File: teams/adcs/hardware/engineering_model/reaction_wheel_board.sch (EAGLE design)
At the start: 81 parts

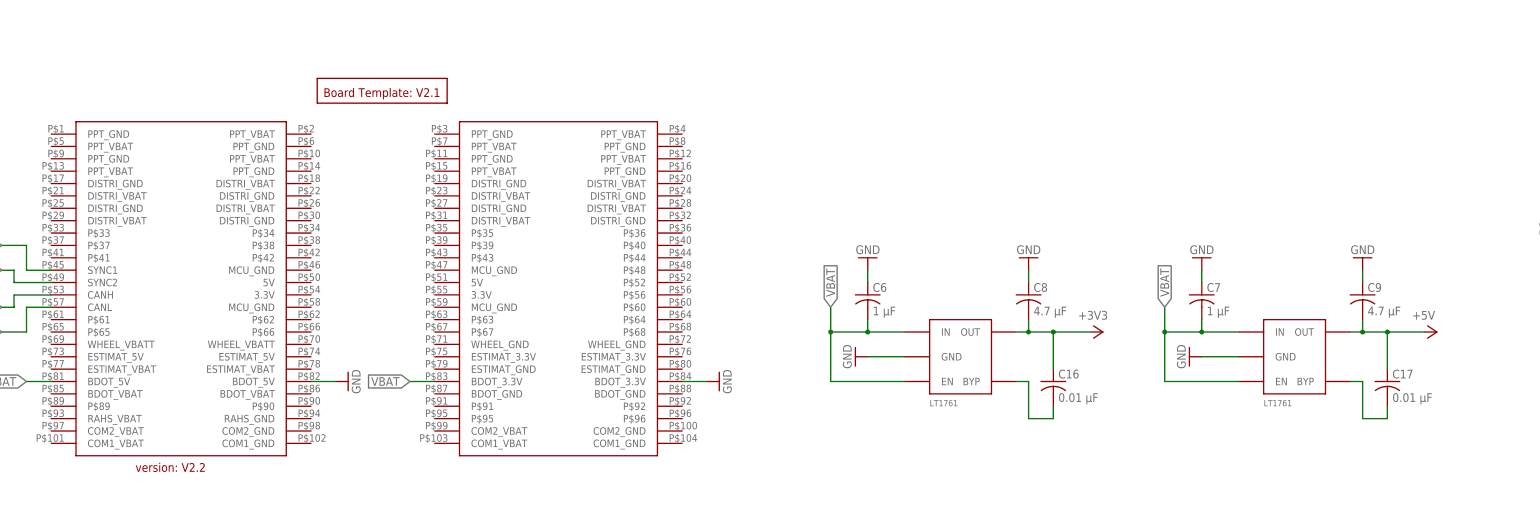
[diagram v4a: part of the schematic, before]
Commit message: ADCS: Fix broken git remote
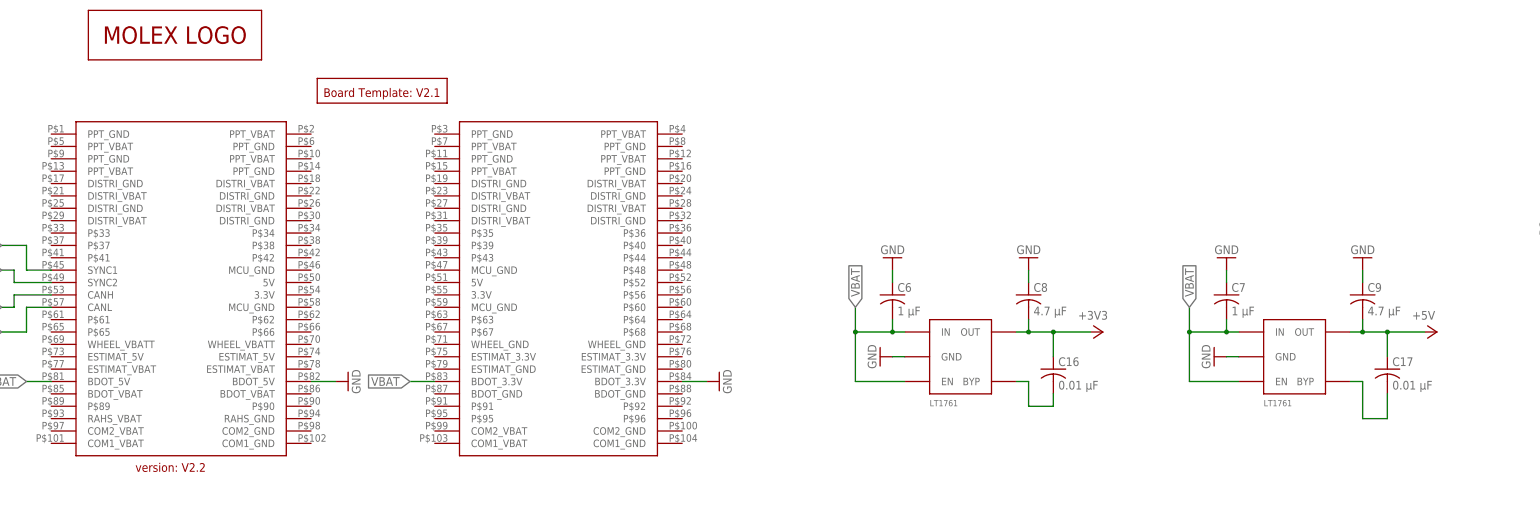
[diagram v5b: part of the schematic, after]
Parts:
- added U$8: LOGO_MOLEX, HuskySat-1 Logos:LOGO_MOLEX
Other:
- moved on the sheet: C16, C17, C6, C7
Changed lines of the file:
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@@
 <?xml version="1.0" encoding="utf-8"?>
 <!DOCTYPE eagle SYSTEM "eagle.dtd">
-<eagle version="8.3.2">
+<eagle version="8.4.1">
 <drawing>
 <settings>
@@
 <layer number="59" name="tCarbon" color="7" fill="1" visible="no" active="no"/>
 <layer number="60" name="bCarbon" color="7" fill="1" visible="no" active="no"/>
+<layer number="88" name="SimResults" color="9" fill="1" visible="yes" active="yes"/>
+<layer number="89" name="SimProbes" color="9" fill="1" visible="yes" active="yes"/>
 <layer number="90" name="Modules" color="5" fill="1" visible="yes" active="yes"/>
 <layer number="91" name="Nets" color="2" fill="1" visible="yes" active="yes"/>
@@
 <part name="C9" library="rcl" library_urn="urn:adsk.eagle:library:334" deviceset="C-US" device="C0805" package3d_urn="urn:adsk.eagle:package:23617/2" value="4.7 μF"/>
 <part name="GND16" library="supply1" library_urn="urn:adsk.eagle:library:371" deviceset="GND" device=""/>
+<part name="U$8" library="HuskySat-1 Logos" deviceset="LOGO_MOLEX" device=""/>
 </parts>
 <sheets>
@@
 <instance part="LDO_3V3" gate="G$1" x="147.32" y="30.48"/>
 <instance part="LDO_5V" gate="G$1" x="215.9" y="30.48"/>
-<instance part="GND38" gate="1" x="193.04" y="30.48" rot="R270"/>
-<instance part="GND39" gate="1" x="124.46" y="30.48" rot="R270"/>
+<instance part="GND38" gate="1" x="198.12" y="30.48" rot="R270"/>
+<instance part="GND39" gate="1" x="129.54" y="30.48" rot="R270"/>
 <instance part="+3V4" gate="G$1" x="175.26" y="35.56" rot="R270"/>
 <instance part="P+4" gate="1" x="243.84" y="35.56" rot="R270"/>
-<instance part="C16" gate="G$1" x="165.1" y="25.4"/>
-<instance part="C17" gate="G$1" x="233.68" y="25.4"/>
+<instance part="C16" gate="G$1" x="165.1" y="27.94"/>
+<instance part="C17" gate="G$1" x="233.68" y="27.94"/>
 <instance part="U$10" gate="G$1" x="147.32" y="-71.12"/>
 <instance part="U$11" gate="G$1" x="210.82" y="-121.92" rot="R270"/>
@@
 <instance part="R14" gate="G$1" x="294.64" y="45.72" rot="R90"/>
 <instance part="GND49" gate="1" x="294.64" y="38.1" rot="MR0"/>
-<instance part="C6" gate="G$1" x="127" y="43.18"/>
-<instance part="GND5" gate="1" x="127" y="50.8" rot="R180"/>
-<instance part="C7" gate="G$1" x="195.58" y="43.18"/>
-<instance part="GND6" gate="1" x="195.58" y="50.8" rot="R180"/>
+<instance part="C6" gate="G$1" x="132.08" y="43.18"/>
+<instance part="GND5" gate="1" x="132.08" y="50.8" rot="R180"/>
+<instance part="C7" gate="G$1" x="200.66" y="43.18"/>
+<instance part="GND6" gate="1" x="200.66" y="50.8" rot="R180"/>
 <instance part="C8" gate="G$1" x="160.02" y="43.18"/>
 <instance part="GND7" gate="1" x="160.02" y="50.8" rot="R180"/>
 <instance part="C9" gate="G$1" x="228.6" y="43.18"/>
 <instance part="GND16" gate="1" x="228.6" y="50.8" rot="R180"/>
+<instance part="U$8" gate="G$1" x="-15.24" y="96.52"/>
 </instances>
 <busses>
@@
 <pinref part="GND39" gate="1" pin="GND"/>
 <pinref part="LDO_3V3" gate="G$1" pin="GND"/>
-<wire x1="127" y1="30.48" x2="134.62" y2="30.48" width="0.1524" layer="91"/>
+<wire x1="132.08" y1="30.48" x2="134.62" y2="30.48" width="0.1524" layer="91"/>
 </segment>
 <segment>
 <pinref part="GND38" gate="1" pin="GND"/>
 <pinref part="LDO_5V" gate="G$1" pin="GND"/>
-<wire x1="195.58" y1="30.48" x2="203.2" y2="30.48" width="0.1524" layer="91"/>
+<wire x1="200.66" y1="30.48" x2="203.2" y2="30.48" width="0.1524" layer="91"/>
 </segment>
 <segment>
@@
 <pinref part="C6" gate="G$1" pin="1"/>
 <pinref part="GND5" gate="1" pin="GND"/>
-<wire x1="127" y1="45.72" x2="127" y2="48.26" width="0.1524" layer="91"/>
+<wire x1="132.08" y1="45.72" x2="132.08" y2="48.26" width="0.1524" layer="91"/>
 </segment>
 <segment>
 <pinref part="C7" gate="G$1" pin="1"/>
 <pinref part="GND6" gate="1" pin="GND"/>
-<wire x1="195.58" y1="45.72" x2="195.58" y2="48.26" width="0.1524" layer="91"/>
+<wire x1="200.66" y1="45.72" x2="200.66" y2="48.26" width="0.1524" layer="91"/>
 </segment>
 <segment>
@@
 <segment>
 <pinref part="LDO_3V3" gate="G$1" pin="IN"/>
-<wire x1="134.62" y1="35.56" x2="127" y2="35.56" width="0.1524" layer="91"/>
-<wire x1="127" y1="35.56" x2="119.38" y2="35.56" width="0.1524" layer="91"/>
-<wire x1="119.38" y1="35.56" x2="119.38" y2="40.64" width="0.1524" layer="91"/>
-<label x="119.38" y="40.64" size="1.778" layer="95" rot="R90" xref="yes"/>
-<junction x="119.38" y="35.56"/>
+<wire x1="134.62" y1="35.56" x2="132.08" y2="35.56" width="0.1524" layer="91"/>
+<wire x1="132.08" y1="35.56" x2="124.46" y2="35.56" width="0.1524" layer="91"/>
+<wire x1="124.46" y1="35.56" x2="124.46" y2="40.64" width="0.1524" layer="91"/>
+<label x="124.46" y="40.64" size="1.778" layer="95" rot="R90" xref="yes"/>
+<junction x="124.46" y="35.56"/>
 <pinref part="LDO_3V3" gate="G$1" pin="EN"/>
-<wire x1="119.38" y1="35.56" x2="119.38" y2="25.4" width="0.1524" layer="91"/>
-<wire x1="119.38" y1="25.4" x2="134.62" y2="25.4" width="0.1524" layer="91"/>
+<wire x1="124.46" y1="35.56" x2="124.46" y2="25.4" width="0.1524" layer="91"/>
+<wire x1="124.46" y1="25.4" x2="134.62" y2="25.4" width="0.1524" layer="91"/>
 <pinref part="C6" gate="G$1" pin="2"/>
-<wire x1="127" y1="35.56" x2="127" y2="38.1" width="0.1524" layer="91"/>
-<junction x="127" y="35.56"/>
+<wire x1="132.08" y1="35.56" x2="132.08" y2="38.1" width="0.1524" layer="91"/>
+<junction x="132.08" y="35.56"/>
 </segment>
 <segment>
 <pinref part="LDO_5V" gate="G$1" pin="IN"/>
-<wire x1="203.2" y1="35.56" x2="195.58" y2="35.56" width="0.1524" layer="91"/>
-<wire x1="195.58" y1="35.56" x2="187.96" y2="35.56" width="0.1524" layer="91"/>
-<wire x1="187.96" y1="35.56" x2="187.96" y2="40.64" width="0.1524" layer="91"/>
-<label x="187.96" y="40.64" size="1.778" layer="95" rot="R90" xref="yes"/>
-<junction x="187.96" y="35.56"/>
+<wire x1="203.2" y1="35.56" x2="200.66" y2="35.56" width="0.1524" layer="91"/>
+<wire x1="200.66" y1="35.56" x2="193.04" y2="35.56" width="0.1524" layer="91"/>
+<wire x1="193.04" y1="35.56" x2="193.04" y2="40.64" width="0.1524" layer="91"/>
+<label x="193.04" y="40.64" size="1.778" layer="95" rot="R90" xref="yes"/>
+<junction x="193.04" y="35.56"/>
 <pinref part="LDO_5V" gate="G$1" pin="EN"/>
-<wire x1="187.96" y1="35.56" x2="187.96" y2="25.4" width="0.1524" layer="91"/>
-<wire x1="187.96" y1="25.4" x2="203.2" y2="25.4" width="0.1524" layer="91"/>
+<wire x1="193.04" y1="35.56" x2="193.04" y2="25.4" width="0.1524" layer="91"/>
+<wire x1="193.04" y1="25.4" x2="203.2" y2="25.4" width="0.1524" layer="91"/>
 <pinref part="C7" gate="G$1" pin="2"/>
-<wire x1="195.58" y1="35.56" x2="195.58" y2="38.1" width="0.1524" layer="91"/>
-<junction x="195.58" y="35.56"/>
+<wire x1="200.66" y1="35.56" x2="200.66" y2="38.1" width="0.1524" layer="91"/>
+<junction x="200.66" y="35.56"/>
 </segment>
 <segment>
@@
 <wire x1="160.02" y1="35.56" x2="165.1" y2="35.56" width="0.1524" layer="91"/>
 <wire x1="165.1" y1="35.56" x2="172.72" y2="35.56" width="0.1524" layer="91"/>
-<wire x1="165.1" y1="27.94" x2="165.1" y2="35.56" width="0.1524" layer="91"/>
+<wire x1="165.1" y1="30.48" x2="165.1" y2="35.56" width="0.1524" layer="91"/>
 <junction x="165.1" y="35.56"/>
 <pinref part="C8" gate="G$1" pin="2"/>
@@
 <wire x1="228.6" y1="35.56" x2="233.68" y2="35.56" width="0.1524" layer="91"/>
 <wire x1="233.68" y1="35.56" x2="241.3" y2="35.56" width="0.1524" layer="91"/>
-<wire x1="233.68" y1="27.94" x2="233.68" y2="35.56" width="0.1524" layer="91"/>
+<wire x1="233.68" y1="30.48" x2="233.68" y2="35.56" width="0.1524" layer="91"/>
 <junction x="233.68" y="35.56"/>
 <pinref part="C9" gate="G$1" pin="2"/>
@@
 <pinref part="C17" gate="G$1" pin="2"/>
 <wire x1="228.6" y1="17.78" x2="233.68" y2="17.78" width="0.1524" layer="91"/>
-<wire x1="233.68" y1="17.78" x2="233.68" y2="20.32" width="0.1524" layer="91"/>
+<wire x1="233.68" y1="17.78" x2="233.68" y2="22.86" width="0.1524" layer="91"/>
 </segment>
 </net>
@@
 <pinref part="LDO_3V3" gate="G$1" pin="BYP"/>
 <wire x1="157.48" y1="25.4" x2="160.02" y2="25.4" width="0.1524" layer="91"/>
-<wire x1="160.02" y1="25.4" x2="160.02" y2="17.78" width="0.1524" layer="91"/>
+<wire x1="160.02" y1="25.4" x2="160.02" y2="20.32" width="0.1524" layer="91"/>
 <pinref part="C16" gate="G$1" pin="2"/>
-<wire x1="160.02" y1="17.78" x2="165.1" y2="17.78" width="0.1524" layer="91"/>
-<wire x1="165.1" y1="17.78" x2="165.1" y2="20.32" width="0.1524" layer="91"/>
-</segment>
-</net>
+<wire x1="160.02" y1="20.32" x2="165.1" y2="20.32" width="0.1524" layer="91"/>
+<wire x1="165.1" y1="20.32" x2="165.1" y2="22.86" width="0.1524" layer="91"/>
+</segment>
+</net>
